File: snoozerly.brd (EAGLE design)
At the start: 70 x 43 mm, 57 parts, among them Q2 MOSFET-NCHANNELFDD8780, Q3 MOSFET-NCHANNELBSS123LT1G, Q4 MOSFET-NCHANNELBSS123LT1G, U1 ATMEGA328P, Y1 32KHz, Y2 8MHz

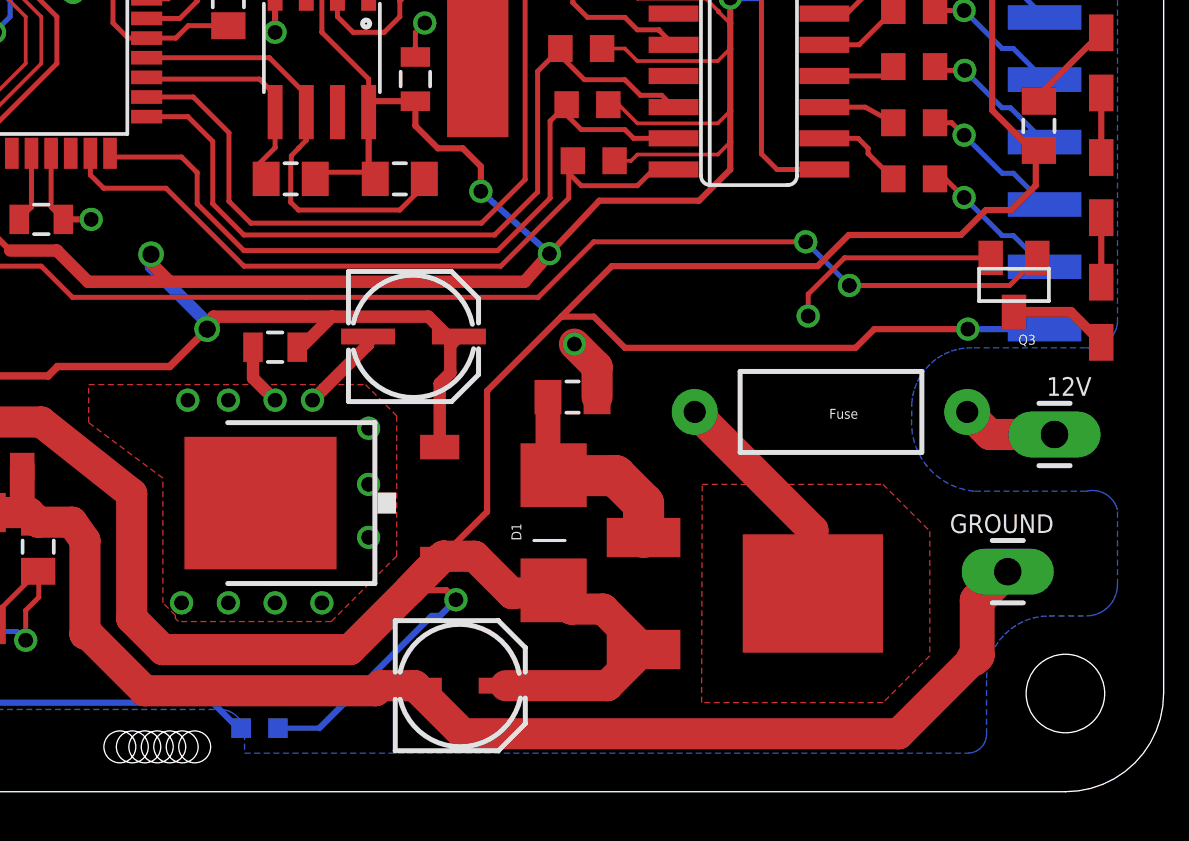
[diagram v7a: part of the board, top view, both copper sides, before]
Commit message: updated vreg pinouts/footprint and rerouted traces
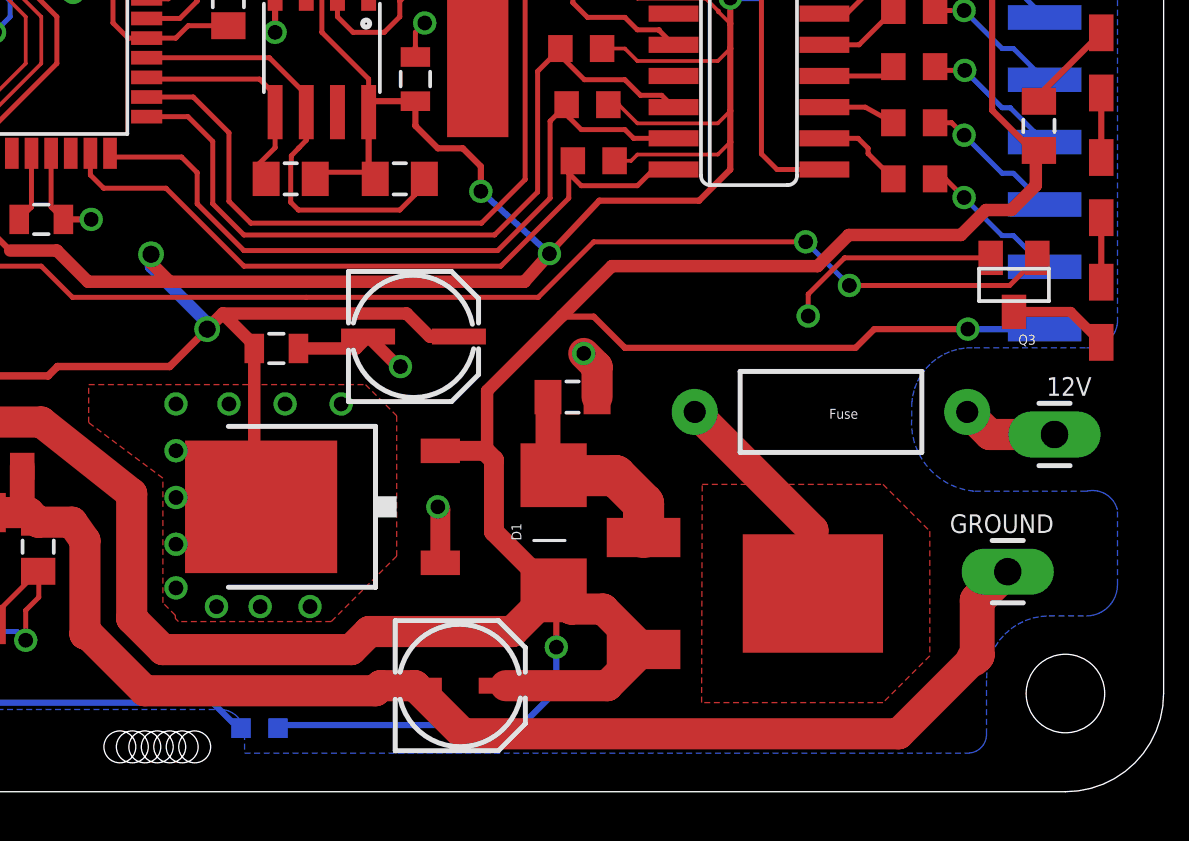
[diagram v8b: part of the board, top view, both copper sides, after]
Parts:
- removed VREG: NCP1117, adafruit:TO252
- added U$26: VREG-3.3VNCP1117, jt_parts:TO-252
- moved C8 0.07 mm to (34.3, 18.5), turned to 0 degrees
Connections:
- net 12V: now also U$26.3; no longer VREG.1
- net 5V: now also U$26.2; no longer VREG.2
- net GND: now also U$26.1; no longer VREG.3
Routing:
- net 12V: track 175.2 -> 179.7 mm
- net 5V: track 191.2 -> 192.8 mm
- net GND: track 111.3 -> 111.9 mm, vias 21 -> 12
- added copper zone on layer 1, net 5V
- removed copper zone on layer 1, net GND
